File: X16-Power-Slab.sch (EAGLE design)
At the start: 17 parts, among them J1 CONN_796636-3, J2 CONN_796636-3, J3 CONN_ET60T, U1 LINEAR_AZ1117CR-3.3TRG1DIODES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

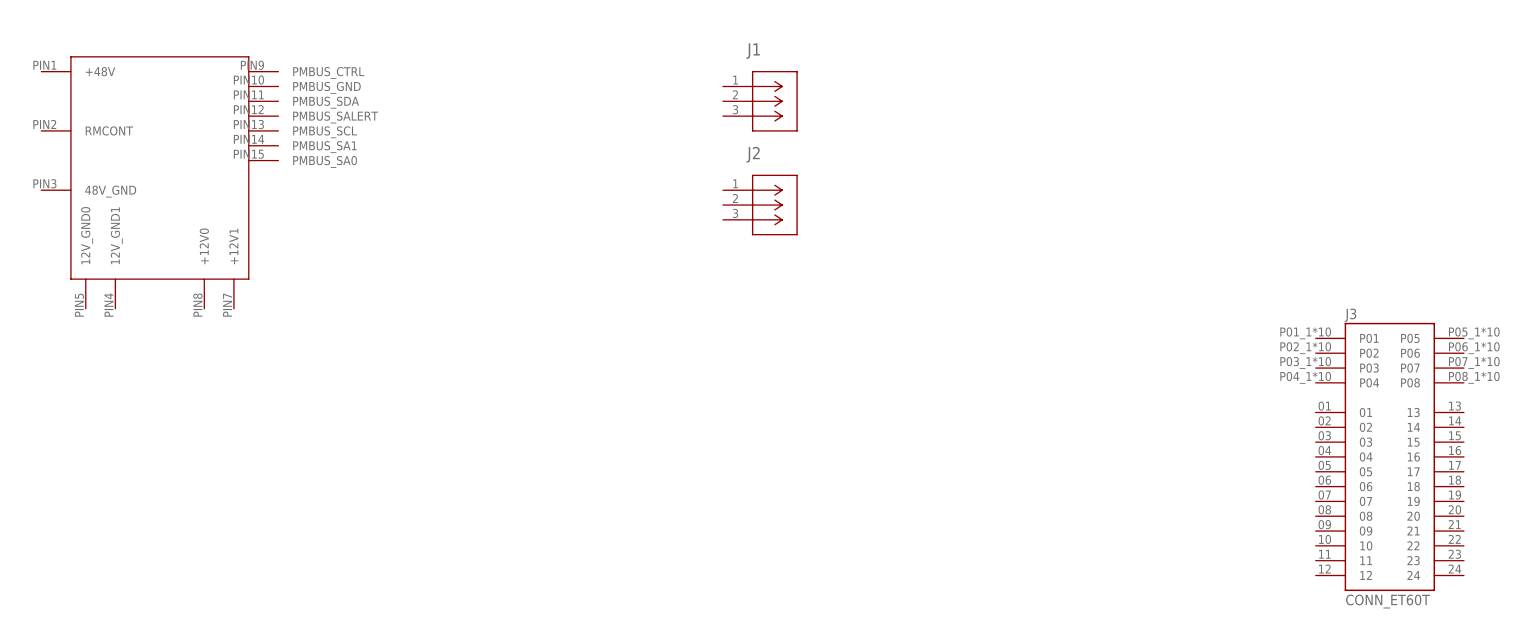
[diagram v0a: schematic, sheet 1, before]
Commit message: Power Conversion finished, updated Brickstribution
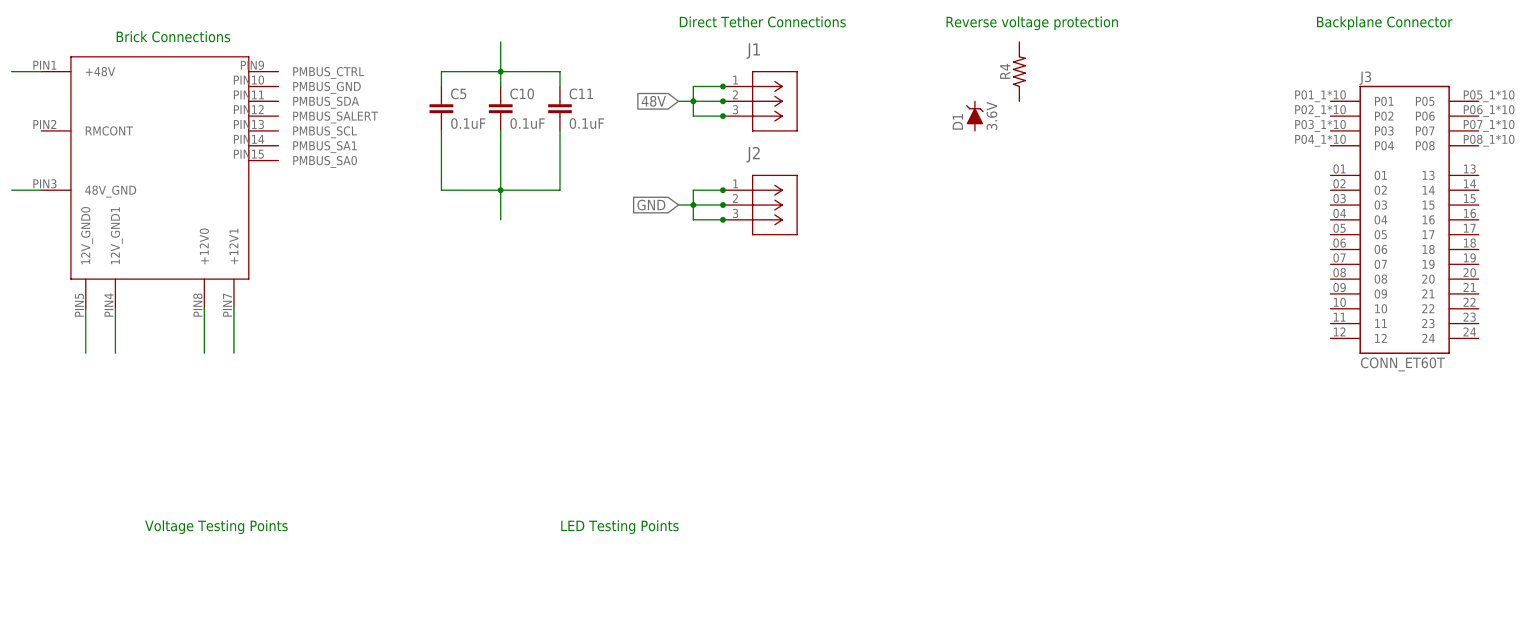
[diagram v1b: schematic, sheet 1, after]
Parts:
- removed D2: 1A/23V/620mV, SparkFun-DiscreteSemi:DIODE-SCHOTTKY-BAT20J
- added C10, C11, C3, C4, C5: 0.1uF, SparkFun-Capacitors:0.1UF-0603-25V-(+80/-20%)
- added D1: 3.6V, SparkFun-DiscreteSemi:DIODE-ZENER-BZT52C3V6S
- added R4: (no value), SparkFun-Resistors:RESISTOR0603
- added U$3: CDBG520-G, X15-Conversion-Parts-Library:CDBG520-G
- R3: value (none) -> 12.4k
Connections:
- net N$9 renamed 12V/2.1A
- new net 48V: J1.1, J1.2, J1.3
- new net GND/2.2D: C1.2, C6.-, C7.-, C8.-, C9.-, R3.1, U$2.GND, U$3.2
- new net N$10: U$1.12V_GND0
- new net N$12: U$1.+12V0
- new net N$13: U$1.+12V1
- new net N$14: U$1.48V_GND
- new net N$15: U$1.+48V
- new net N$16: C10.1, C11.1, C5.1
- new net N$17: C10.2, C11.2, C5.2
- new net N$3: C3.1, U1.INPUT
- new net N$5: U1.GND
- new net N$6: C4.1, U1.OUPUT
- new net N$7: C3.2
- new net N$9: C4.2
- net GND: now also J2.1, J2.2, J2.3
- net N$11: now also U$1.12V_GND1; no longer C1.2, C6.-, C7.-, C8.-, C9.-, D2.A, R3.1, U$2.GND
- net N$2: now also U$3.1
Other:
- note added: "Backplane Connector"
- note added: "Brick Connections"
- note added: "Direct Tether Connections"
- note added: "LED Testing Points"
- note added: "Reverse voltage protection"
- note added: "Voltage Testing Points"
- moved on the sheet: J3

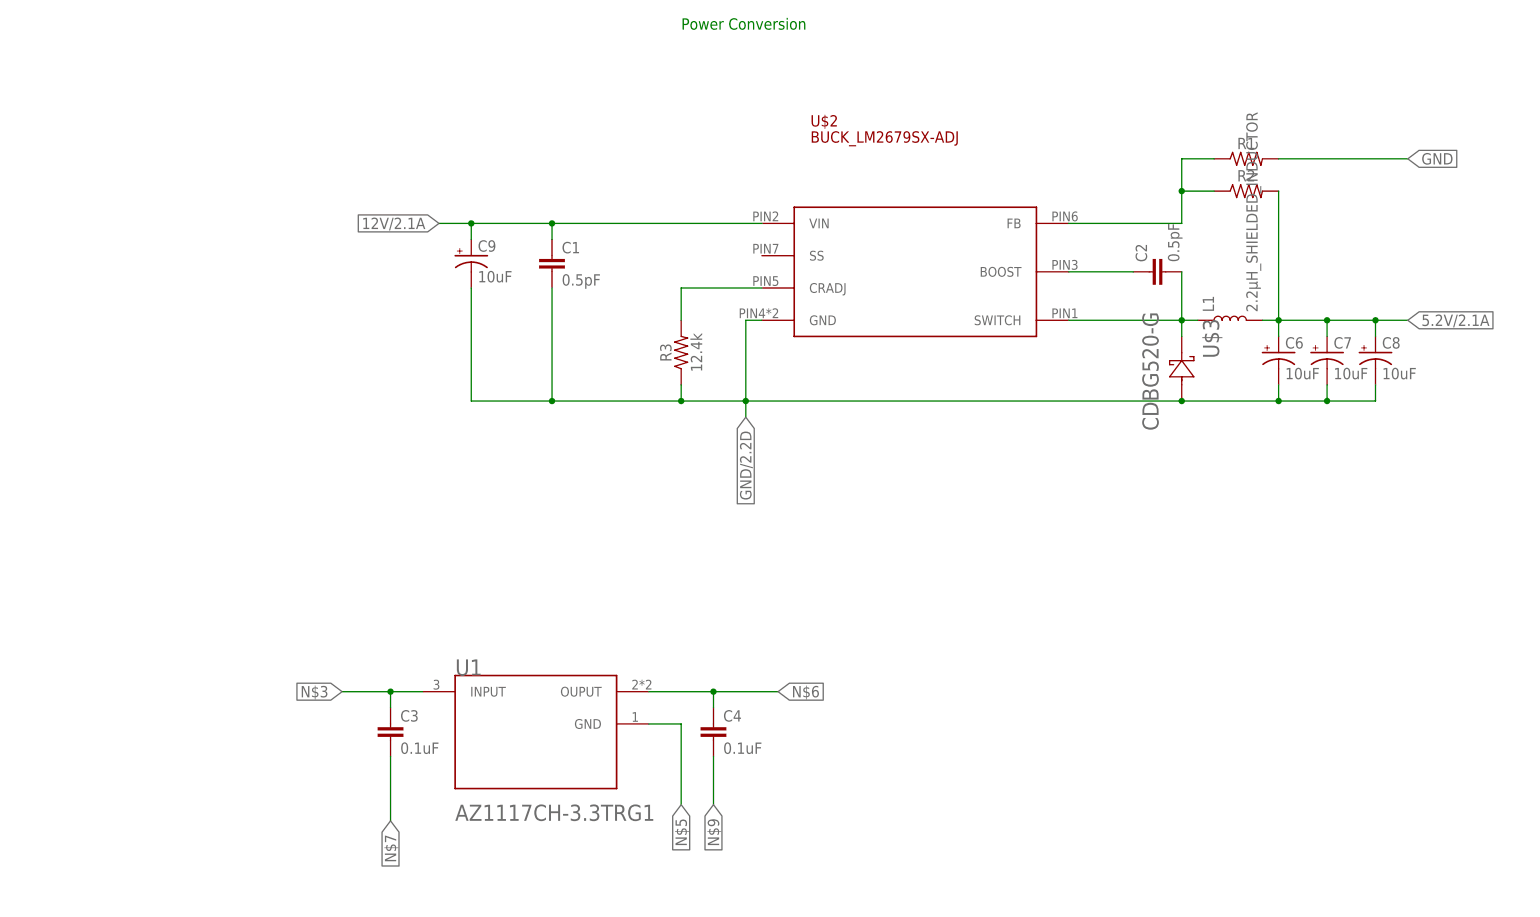
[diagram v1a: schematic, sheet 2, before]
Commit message: Updated component values, added test points
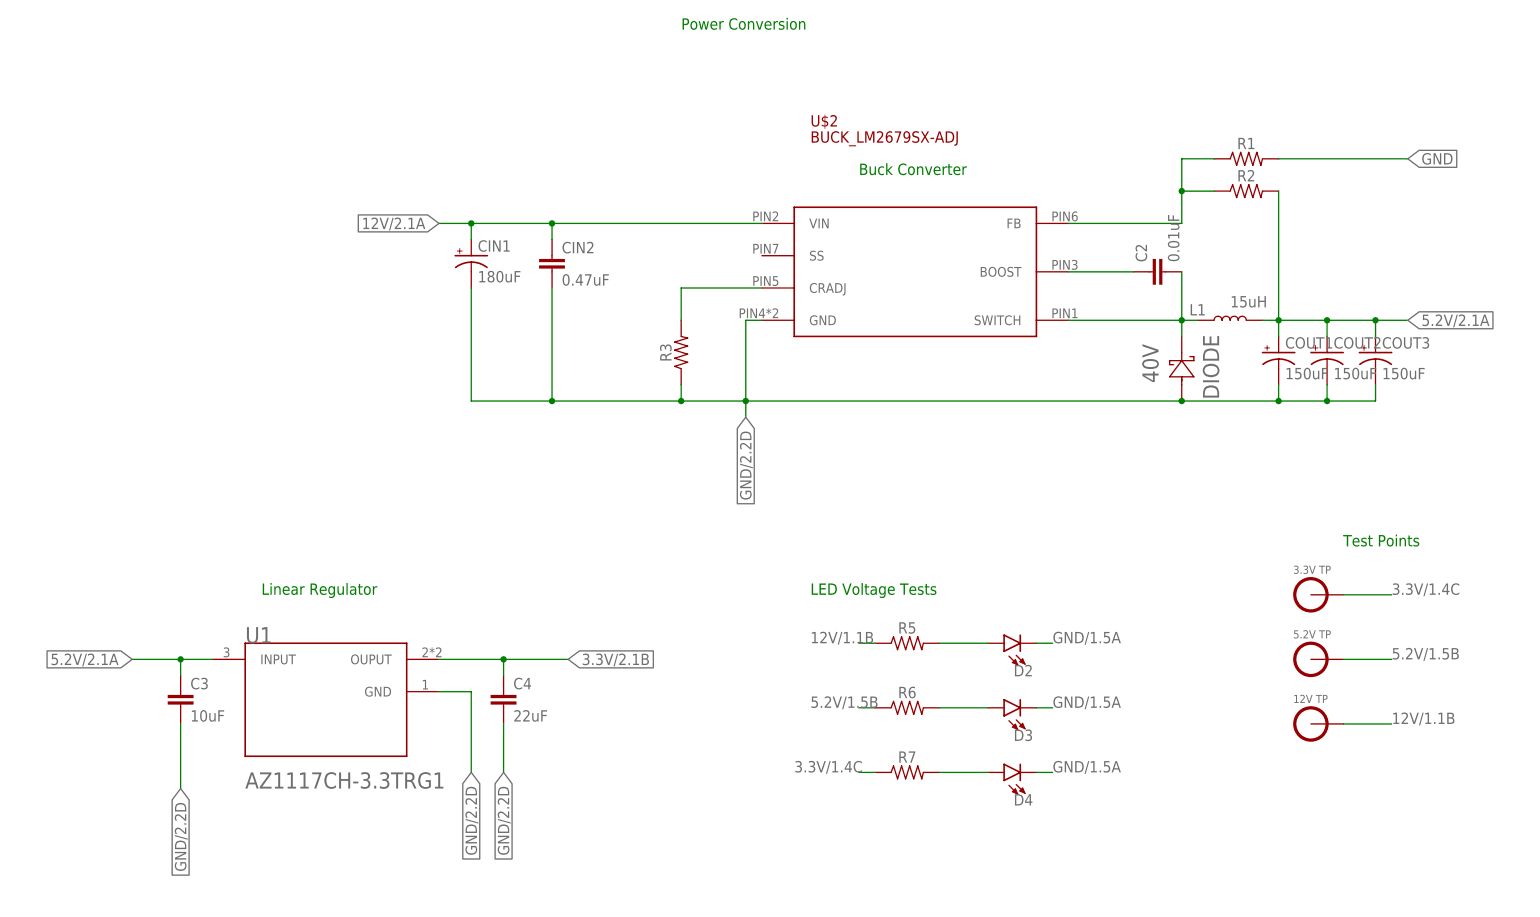
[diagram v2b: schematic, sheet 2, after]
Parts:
- removed C1: 0.5pF, SparkFun-Capacitors:0.5PF-0402_TIGHT-50V-PM0.05PF-NP0
- added CIN2: 0.47uF, SparkFun-Capacitors:0.1UF-0603-25V-(+80/-20%)
- added D2, D3, D4: (no value), SparkFun-LED:LED0603
- added DIODE: 40V, X15-Conversion-Parts-Library:CDBG520-G
- added R5, R6, R7: (no value), SparkFun-Resistors:RESISTOR0603
- added U$4: 5.2V_TESTPOINT, X15-Conversion-Parts-Library:5.2V_TESTPOINT
- added U$5: 12V_TESTPOINT, X15-Conversion-Parts-Library:12V_TESTPOINT
- C2: value 0.5pF -> 0.01uF; device SparkFun-Capacitors:0.5PF-0402_TIGHT-50V-PM0.05PF-NP0 -> SparkFun-Capacitors:0.1UF-0603-25V-(+80/-20%)
- C3: value 0.1uF -> 10uF
- C4: value 0.1uF -> 22uF
- CIN1: value 10uF -> 180uF
- COUT1, COUT2, COUT3: value 10uF -> 150uF
- L1: value 2.2μH_SHIELDED_INDUCTOR -> 15uH
- R3: value 12.4k -> (none)
- U$3: value CDBG520-G -> 3.3V_TESTPOINT; device X15-Conversion-Parts-Library:CDBG520-G -> X15-Conversion-Parts-Library:3.3V_TESTPOINT
- renumbered C6 to COUT1, C7 to COUT2, C8 to COUT3, C9 to CIN1
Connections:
- net N$6 renamed 3.3V/2.1B
- removed net N$7: C3.2
- removed net N$9: C4.2
- new net 12V/1.1B: R5.1, U$5.12V
- new net 3.3V/1.4C: R7.1, U$3.3.3V
- new net 5.2V/1.5B: R6.1, U$4.5.2V
- new net GND/1.5A: D2.C, D3.C, D4.C
- new net N$6: D4.A, R7.2
- net 12V/2.1A: now also CIN2.1; no longer C1.1
- net 5.2V/2.1A: now also C3.1, U1.INPUT
- net GND/2.2D: now also C3.2, C4.2, CIN2.2, DIODE.2, U1.GND; no longer C1.2, U$3.2
- net N$2: now also DIODE.1; no longer U$3.1
- net N$3: now also D2.A, R5.2; no longer C3.1, U1.INPUT
- net N$5: now also D3.A, R6.2; no longer U1.GND
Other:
- note added: "Buck Converter"
- note added: "LED Voltage Tests"
- note added: "Linear Regulator"
- note added: "Test Points"
- moved on the sheet: C3, C4, U1
